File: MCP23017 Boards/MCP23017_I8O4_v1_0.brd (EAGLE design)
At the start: 90 x 90 mm, 71 parts, among them IC3 74HC540N, IC4 74HC540N, IC5 MCP23017SP, X4 057-016-0

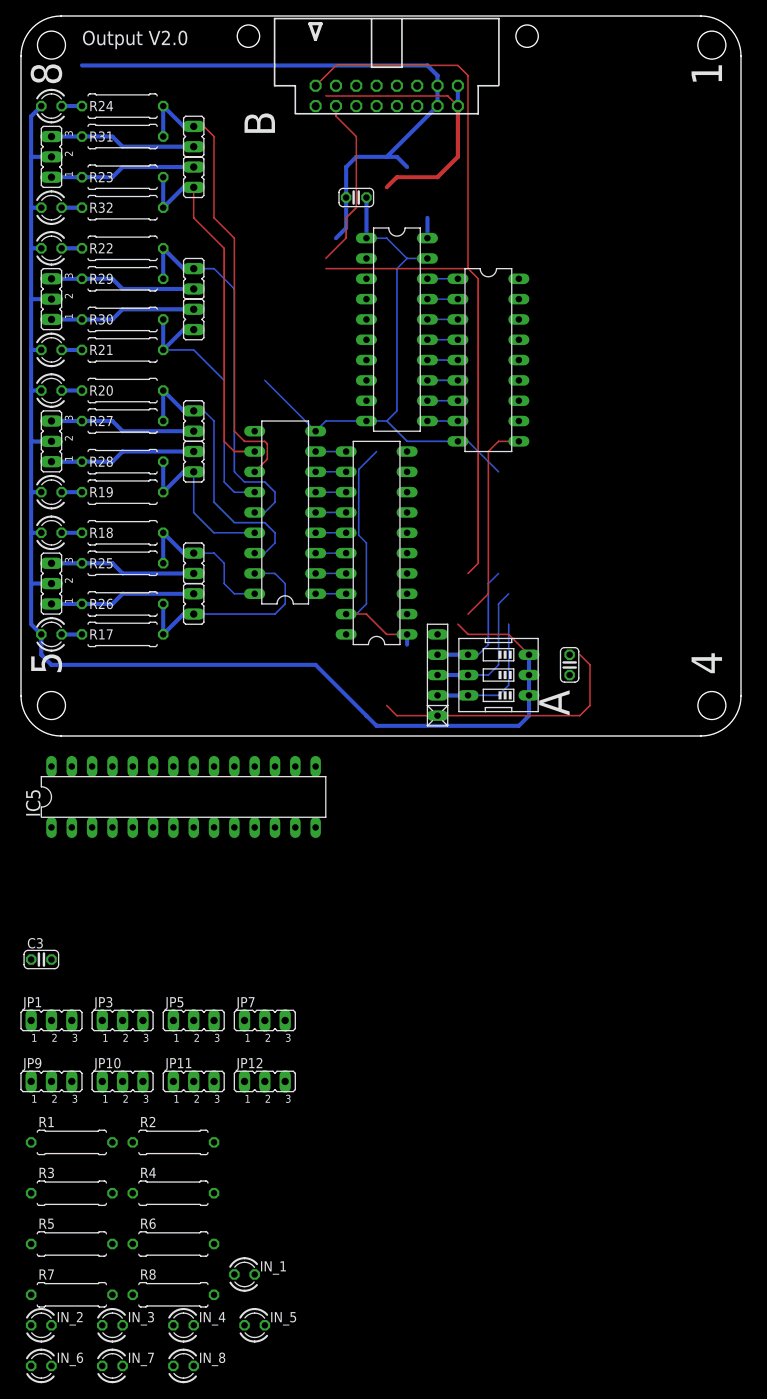
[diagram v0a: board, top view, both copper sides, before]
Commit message: Update MCP23017_I8O4_v1_0.brd
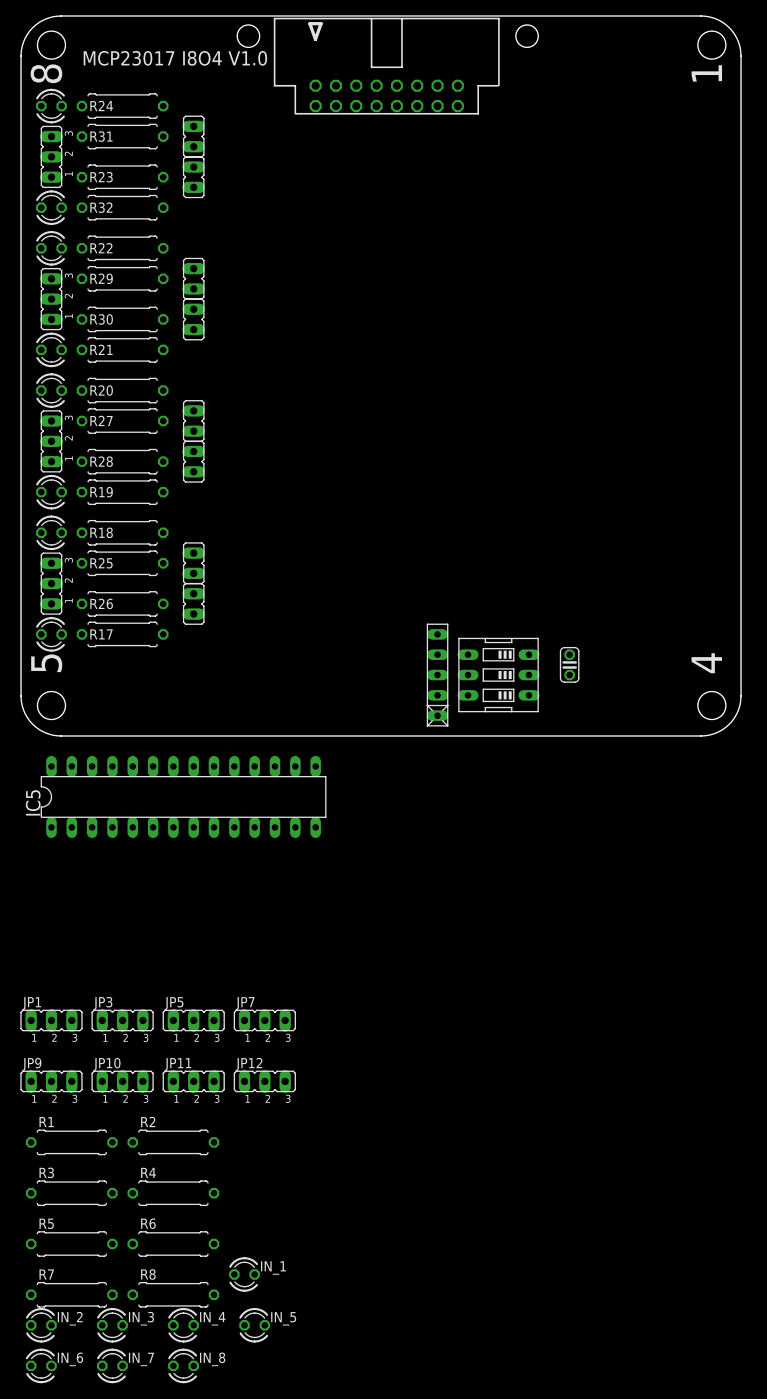
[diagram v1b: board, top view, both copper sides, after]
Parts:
- removed C3, C6: 100nF, resistor:C025-024X044
- removed IC1, IC2: (no value), uln-udn:DIL18
- removed IC3, IC4: 74HC540N, 74xx-eu:DIL20
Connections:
- removed net N$1: IC2.18, IN_1.K, JP1.3
- removed net N$12: IC2.8, IC3.11
- removed net N$14: IC2.7, IC3.12
- removed net N$15: IC2.6, IC3.13
- removed net N$16: IC2.5, IC3.14
- removed net N$17: IC2.4, IC3.15
- removed net N$18: IC2.3, IC3.16
- removed net N$19: IC2.2, IC3.17
- removed net N$20: IC2.1, IC3.18
- removed net N$22: IC3.3, IC5.22
- removed net N$24: IC3.5, IC5.24
- removed net N$26: IC3.7, IC5.26
- removed net N$28: IC3.9, IC5.28
- removed net N$3: IC2.16, IN_3.K, JP5.3
- removed net N$34: IC1.8, IC4.11
- removed net N$39: IC1.7, IC4.12
- removed net N$40: IC1.6, IC4.13
- removed net N$44: IC1.5, IC4.14
- removed net N$45: IC1.4, IC4.15
- removed net N$46: IC1.3, IC4.16
- removed net N$47: IC1.2, IC4.17
- removed net N$48: IC1.1, IC4.18
- removed net N$49: IC4.2, IC5.1
- removed net N$5: IC2.14, IN_5.K, JP9.3
- removed net N$51: IC4.4, IC5.3
- removed net N$55: IC4.6, IC5.5
- removed net N$57: IC4.8, IC5.7
- removed net N$60: IC1.17, JP24.2, R17.2, R26.1
- removed net N$64: IC1.15, JP19.2, R19.2, R28.1
- removed net N$68: IC1.13, JP21.2, R21.2, R30.1
- removed net N$8: IC2.12, IN_7.K, JP11.3
- removed net N$83: IC1.11, JP23.2, R23.2, R32.1
- net GND2: no longer C3.1, C6.1, IC1.9, IC2.9, IC3.1, IC3.10, IC3.19, IC4.1, IC4.10, IC4.19
- net N$2: now also IC5.22; no longer IC2.17
- net N$21: now also IN_1.K, JP1.3; no longer IC3.2
- net N$23: now also IN_3.K, JP5.3; no longer IC3.4
- net N$25: now also IN_5.K, JP9.3; no longer IC3.6
- net N$27: now also IN_7.K, JP11.3; no longer IC3.8
- net N$4: now also IC5.24; no longer IC2.15
- net N$50: now also JP24.2, R17.2, R26.1; no longer IC4.3
- net N$52: now also JP19.2, R19.2, R28.1; no longer IC4.5
- net N$56: now also JP21.2, R21.2, R30.1; no longer IC4.7
- net N$58: now also JP23.2, R23.2, R32.1; no longer IC4.9
- net N$59: now also IC5.1; no longer IC1.18
- net N$63: now also IC5.3; no longer IC1.16
- net N$65: now also IC5.5; no longer IC1.14
- net N$7: now also IC5.26; no longer IC2.13
- net N$71: now also IC5.7; no longer IC1.12
- net N$9: now also IC5.28; no longer IC2.11
- net VCC5.1: no longer C3.2, C6.2, IC1.10, IC2.10, IC3.20, IC4.20
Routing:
- net VCC5.1: track 274.8 -> 0.00 mm
- net GND2: track 173.2 -> 0.00 mm
- net N$82: track 101.7 -> 0.00 mm
- net N$71: track 58.5 -> 0.00 mm
- net N$65: track 48.1 -> 0.00 mm
- net N$83: track 46.3 -> 0.00 mm
- net N$63: track 35.4 -> 0.00 mm
- net N$68: track 34.9 -> 0.00 mm
- net N$60: track 27.5 -> 0.00 mm
- net N$64: track 22.4 -> 0.00 mm
- net N$84: track 21.7 -> 0.00 mm
- net N$59: track 19.9 -> 0.00 mm
- net N$81: track 18.3 -> 0.00 mm
- net N$80: track 18.3 -> 0.00 mm
- net N$79: track 18.3 -> 0.00 mm
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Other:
- board text added: "MCP23017 I8O4 V1.0"
- board text removed: "A"
- board text removed: "B"
- board text removed: "Output V2.0"

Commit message: Update MCP23017_I8O4_v1_0.brd
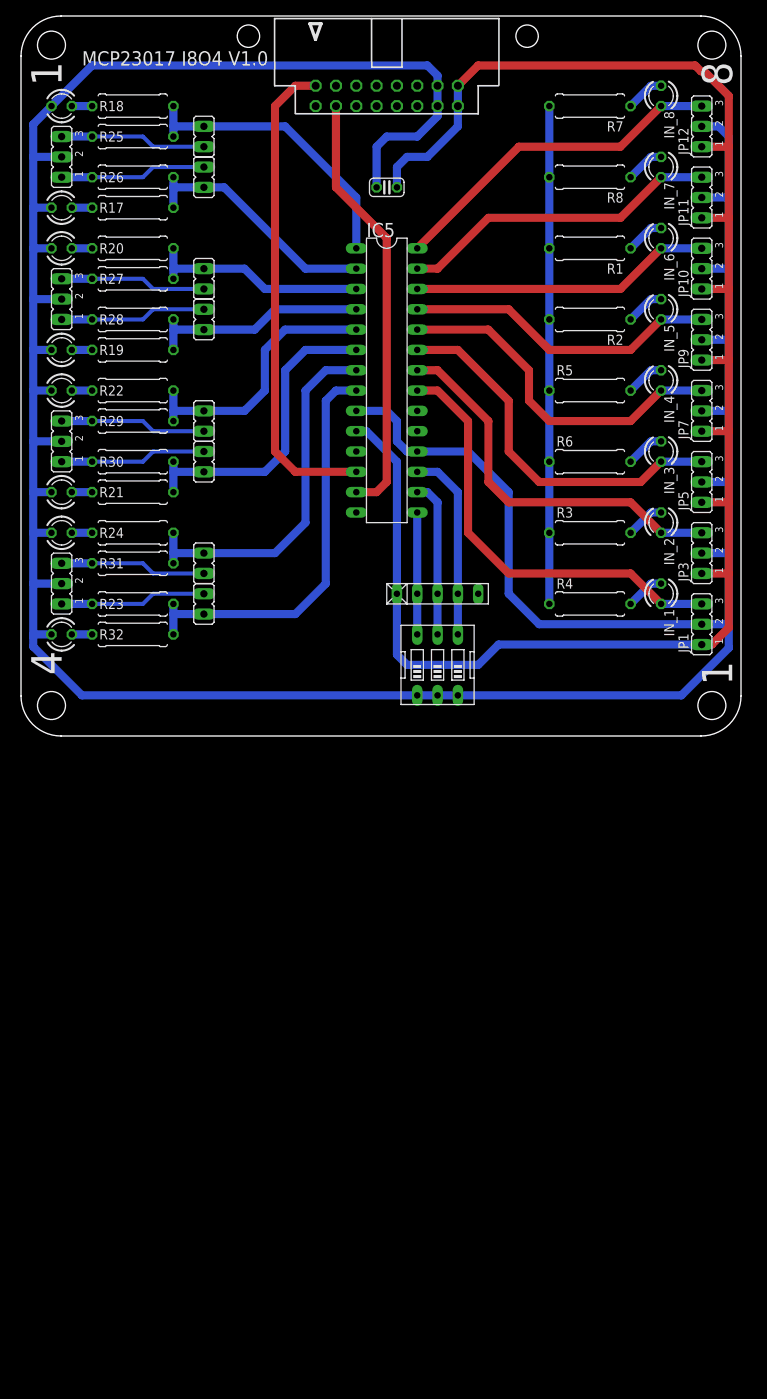
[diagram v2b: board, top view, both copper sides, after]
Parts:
- moved IN_8 169.6 mm to (80.0, 80.0), turned to 270 degrees
- moved IN_7 164.8 mm to (80.0, 71.1), turned to 270 degrees
- moved R7 162.1 mm to (71.1, 78.7), turned to 180 degrees
- moved IN_6 160.9 mm to (80.0, 62.2), turned to 270 degrees
- moved R8 149.1 mm to (71.1, 69.8), turned to 180 degrees
- moved IN_5 136.8 mm to (80.0, 53.3), turned to 270 degrees
- moved IN_4 132.3 mm to (80.0, 44.5), turned to 270 degrees
- moved JP12 131.3 mm to (85.1, 76.2), turned to 90 degrees
- moved R1 129.2 mm to (71.1, 61.0), turned to 180 degrees
- moved IN_3 129.0 mm to (80.0, 35.6), turned to 270 degrees
- moved JP11 127.4 mm to (85.1, 67.3), turned to 90 degrees
- moved IN_2 126.8 mm to (80.0, 26.7), turned to 270 degrees
- moved R5 124.8 mm to (71.1, 43.2)
- moved JP10 124.8 mm to (85.1, 58.4), turned to 90 degrees
- moved JP9 123.3 mm to (85.1, 49.5), turned to 90 degrees
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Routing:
- net VCC5.1: track 0.00 -> 415.8 mm
- net GND2: track 0.00 -> 218.7 mm
- net VCC5.2: track 0.00 -> 62.2 mm
- net N$82: track 0.00 -> 60.5 mm
- net N$21: track 0.00 -> 54.8 mm
- net N$84: track 0.00 -> 54.0 mm
- net N$58: track 0.00 -> 51.6 mm
- net N$2: track 0.00 -> 48.4 mm
- net N$23: track 0.00 -> 47.2 mm
- net N$71: track 0.00 -> 45.8 mm
- net N$4: track 0.00 -> 44.1 mm
- net N$9: track 0.00 -> 42.9 mm
- net N$27: track 0.00 -> 40.3 mm
- net N$25: track 0.00 -> 39.2 mm
- net N$56: track 0.00 -> 38.9 mm
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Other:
- board text removed: "5"

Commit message: Update MCP23017_I8O4_v1_0.brd
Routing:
- net VCC5.1: track 415.8 -> 435.6 mm
- net GND2: track 218.7 -> 229.6 mm
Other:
- board text added: "By Djpredator69"
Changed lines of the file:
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@@
 <text x="5.08" y="81.28" size="3.81" layer="25" rot="R90">1</text>
 <text x="5.08" y="7.62" size="3.81" layer="25" rot="R90">4</text>
+<text x="11.43" y="1.27" size="1.778" layer="25">By Djpredator69</text>
 </plain>
 <attributes>
@@
 <wire x1="85.09" y1="64.77" x2="88.476" y2="64.77" width="1.016" layer="1"/>
 <wire x1="85.09" y1="73.66" x2="88.476" y2="73.66" width="1.016" layer="1"/>
-<wire x1="41.91" y1="38.1" x2="43.18" y2="38.1" width="1.016" layer="16"/>
-<wire x1="46.99" y1="34.29" x2="46.99" y2="17.78" width="1.016" layer="16"/>
-<wire x1="43.18" y1="38.1" x2="46.99" y2="34.29" width="1.016" layer="16"/>
 <wire x1="85.09" y1="11.43" x2="59.69" y2="11.43" width="1.016" layer="16"/>
 <wire x1="59.69" y1="11.43" x2="57.15" y2="8.89" width="1.016" layer="16"/>
@@
 <wire x1="48.26" y1="8.89" x2="46.99" y2="10.16" width="1.016" layer="16"/>
 <wire x1="46.99" y1="10.16" x2="46.99" y2="17.78" width="1.016" layer="16"/>
+<wire x1="41.91" y1="38.1" x2="44.45" y2="38.1" width="0.508" layer="16"/>
+<wire x1="44.45" y1="38.1" x2="46.99" y2="40.64" width="0.508" layer="16"/>
+<wire x1="46.99" y1="40.64" x2="46.99" y2="68.58" width="0.508" layer="16"/>
 </signal>
 <signal name="VCC5.1">
@@
 <wire x1="1.524" y1="25.4" x2="1.524" y2="19.05" width="1.016" layer="16"/>
 <wire x1="1.524" y1="19.05" x2="1.524" y2="12.7" width="1.016" layer="16"/>
-<wire x1="1.524" y1="12.7" x2="1.524" y2="12.446" width="1.016" layer="16"/>
 <wire x1="3.81" y1="25.4" x2="1.524" y2="25.4" width="1.016" layer="16"/>
 <wire x1="3.81" y1="30.48" x2="1.524" y2="30.48" width="1.016" layer="16"/>
@@
 <wire x1="82.55" y1="5.08" x2="88.476" y2="11.006" width="1.016" layer="16"/>
 <wire x1="88.476" y1="11.006" x2="88.476" y2="13.546" width="1.016" layer="16"/>
-<wire x1="1.524" y1="12.446" x2="1.524" y2="11.176" width="1.016" layer="16"/>
+<wire x1="1.524" y1="12.7" x2="1.524" y2="11.176" width="1.016" layer="16"/>
 <wire x1="1.524" y1="11.176" x2="7.62" y2="5.08" width="1.016" layer="16"/>
 <wire x1="7.62" y1="5.08" x2="49.53" y2="5.08" width="1.016" layer="16"/>
@@
 <wire x1="52.07" y1="77.47" x2="49.53" y2="74.93" width="1.016" layer="16"/>
 <wire x1="49.53" y1="35.56" x2="48.26" y2="35.56" width="1.016" layer="16"/>
-<wire x1="48.26" y1="35.56" x2="46.99" y2="36.83" width="1.016" layer="16"/>
-<wire x1="46.99" y1="36.83" x2="46.99" y2="39.37" width="1.016" layer="16"/>
-<wire x1="46.99" y1="39.37" x2="45.72" y2="40.64" width="1.016" layer="16"/>
-<wire x1="45.72" y1="40.64" x2="41.91" y2="40.64" width="1.016" layer="16"/>
 <wire x1="85.09" y1="13.97" x2="64.77" y2="13.97" width="1.016" layer="16"/>
 <wire x1="60.96" y1="17.78" x2="60.96" y2="30.48" width="1.016" layer="16"/>
@@
 <wire x1="64.77" y1="13.97" x2="60.96" y2="17.78" width="1.016" layer="16"/>
 <wire x1="3.81" y1="12.7" x2="1.524" y2="12.7" width="1.016" layer="16"/>
+<wire x1="41.91" y1="40.64" x2="43.18" y2="40.64" width="0.508" layer="16"/>
+<wire x1="43.18" y1="40.64" x2="44.45" y2="41.91" width="0.508" layer="16"/>
+<wire x1="44.45" y1="41.91" x2="44.45" y2="68.58" width="0.508" layer="16"/>
 </signal>
 <signal name="N$59">
